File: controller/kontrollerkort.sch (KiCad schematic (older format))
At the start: 20 parts, among them J1 SPI, J2 SERIAL, J3 POWER, J4 RESET, J5 CONTROL, J6 SENSORS, U1 ATMEGA8

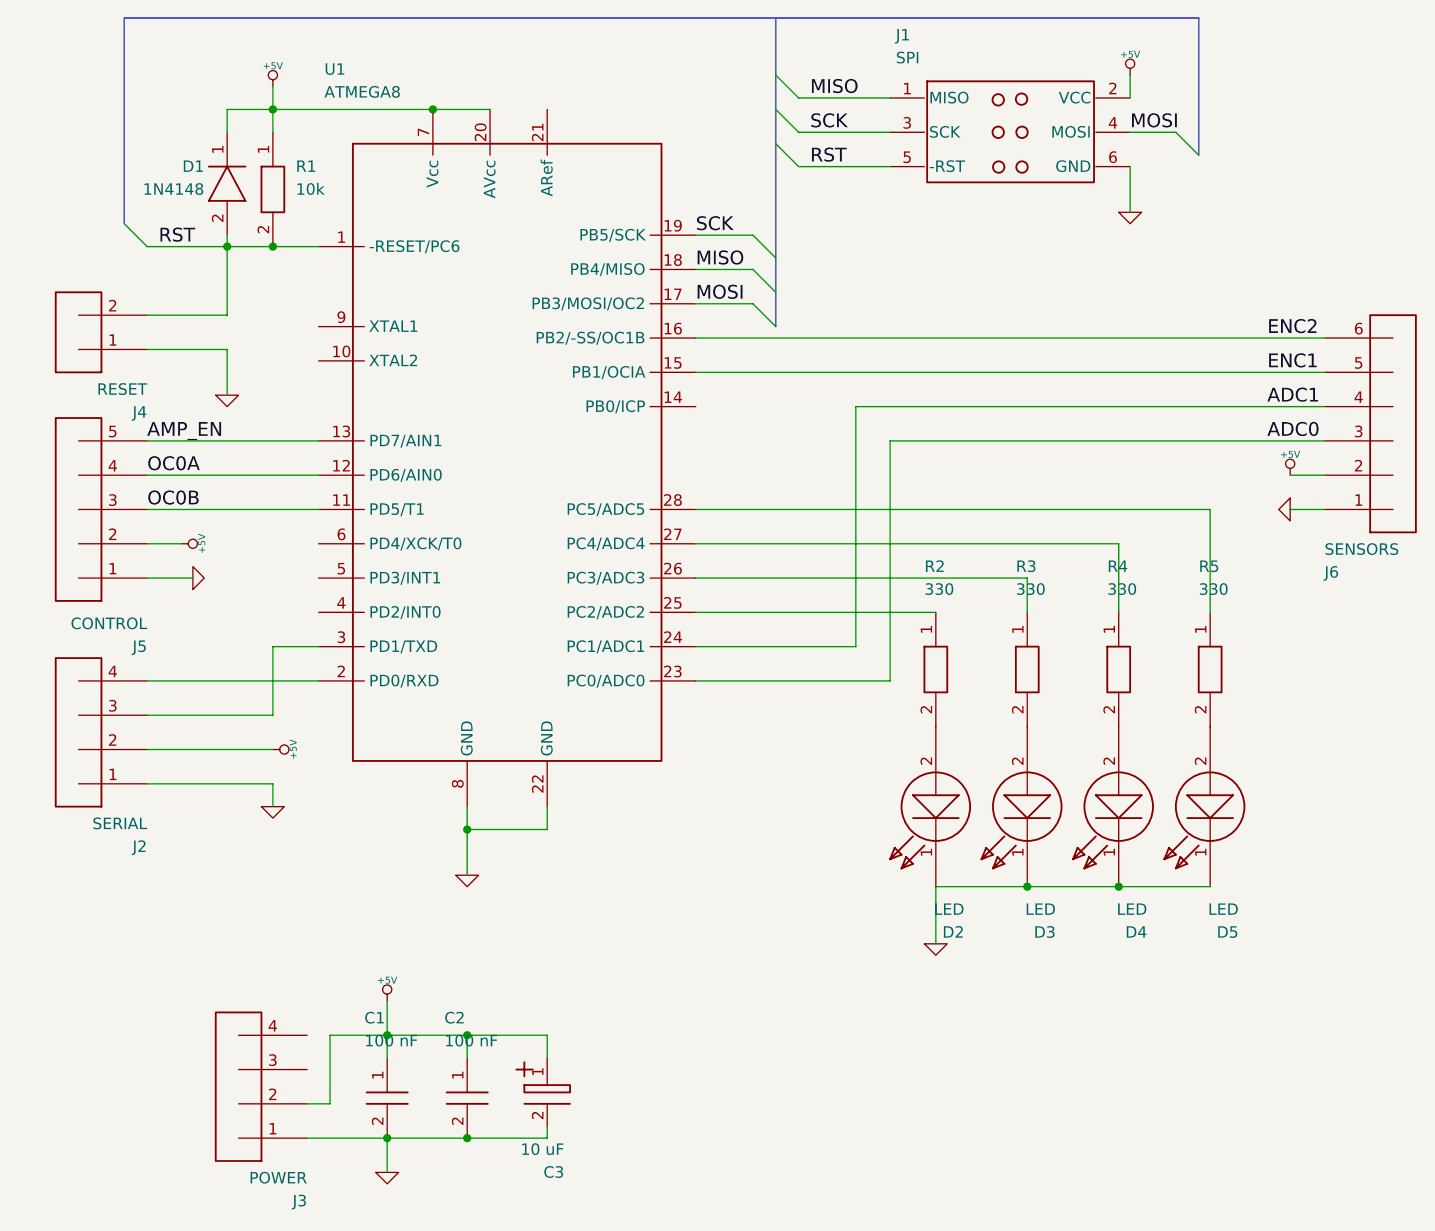
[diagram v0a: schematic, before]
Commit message: Updated controller board. Changed some connector pinouts to simplify board layout.
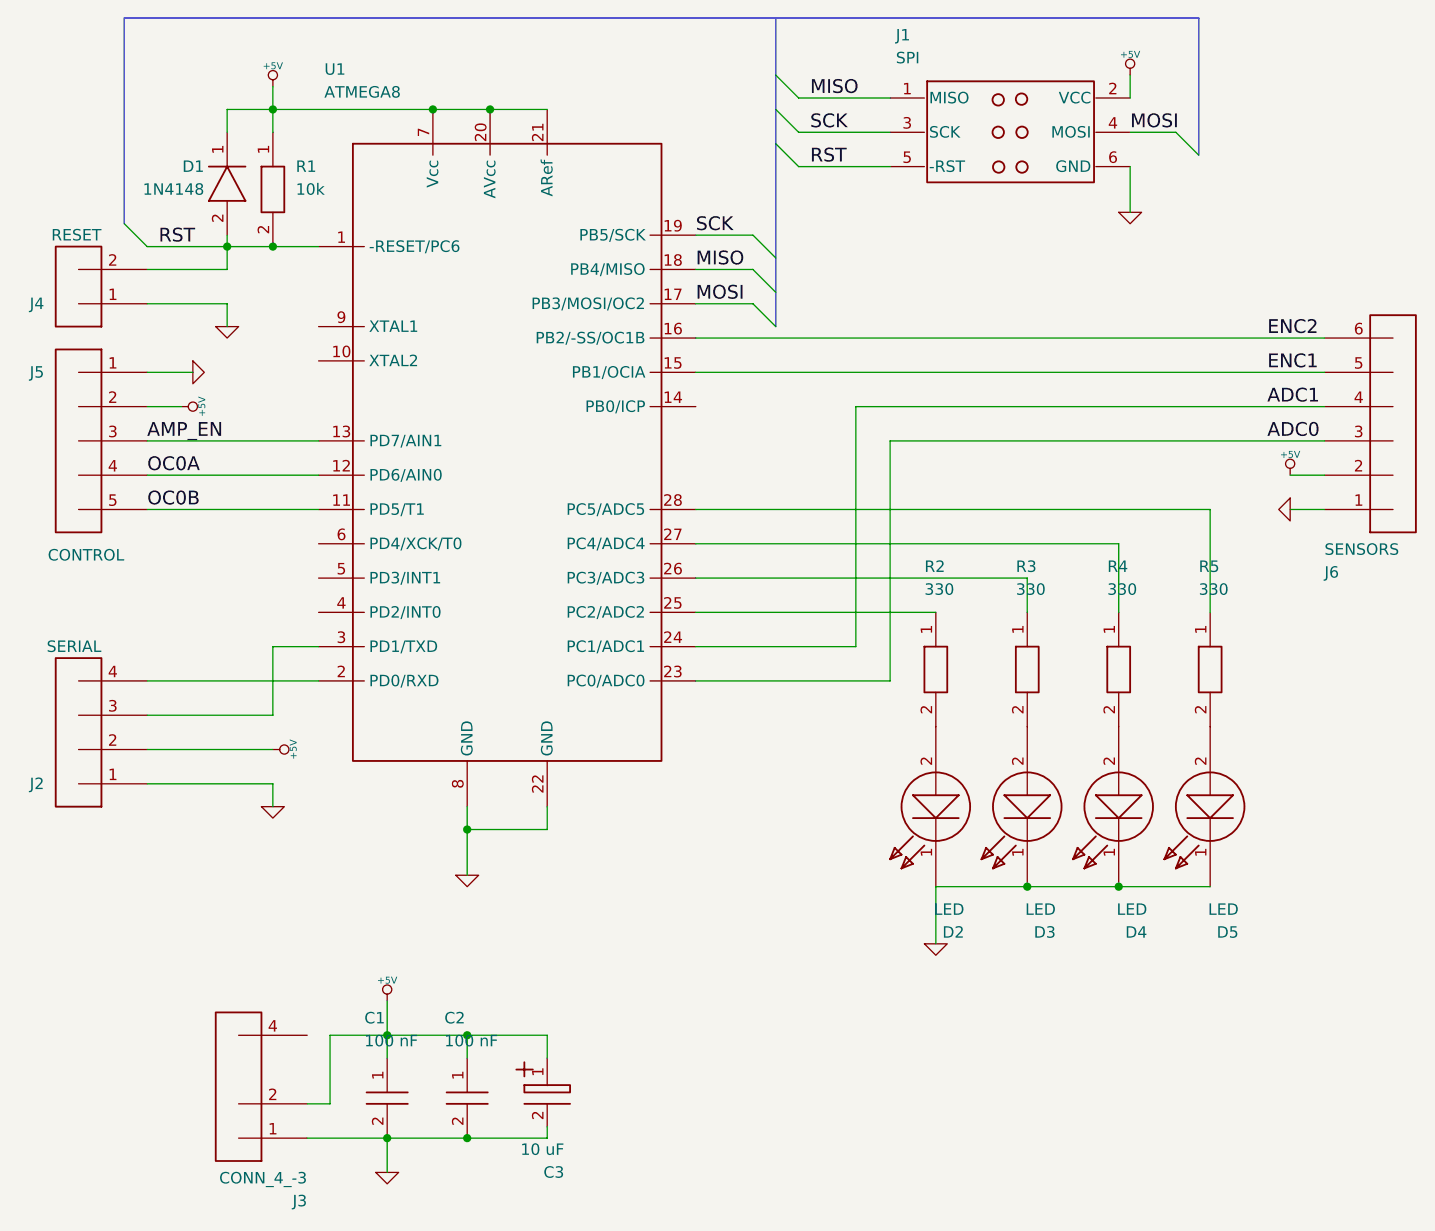
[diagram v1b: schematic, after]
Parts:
- removed J3: POWER, SIP4, symbol CONN_4
- added J3: CONN_4_-3, SIP4_-3, symbol CONN_4_-3
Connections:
- net +5V: now also U1.21 (ARef), J3.2
- net AMP_EN: now also J5.3; no longer J5.5
- net GND: now also J3.1
- net OC0B: now also J5.5; no longer J5.3
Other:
- moved on the sheet: J4, J5
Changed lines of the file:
@@
 LIBS:V_Relay
 LIBS:power
+LIBS:graphic
+LIBS:graphics
 LIBS:kontrollerkort-cache
 EELAYER 27 0
@@
 Sheet 1 1
 Title ""
-Date "7 oct 2014"
+Date "10 oct 2014"
 Rev ""
 Comp ""
@@
 $EndComp
 $Comp
-L +5V #PWR01
+L +5V #PWR4
 U 1 1 5433A0E3
 P 4300 2200
-F 0 "#PWR01" H 4300 2290 20  0001 C CNN
+F 0 "#PWR4" H 4300 2290 20  0001 C CNN
 F 1 "+5V" H 4300 2290 30  0000 C CNN
 F 2 "" H 4300 2200 60  0000 C CNN
@@
 $EndComp
 $Comp
-L GND #PWR02
+L GND #PWR9
 U 1 1 5433A107
 P 5150 5650
-F 0 "#PWR02" H 5150 5650 30  0001 C CNN
+F 0 "#PWR9" H 5150 5650 30  0001 C CNN
 F 1 "GND" H 5150 5580 30  0001 C CNN
 F 2 "" H 5150 5650 60  0000 C CNN
@@
 	6400 2850 6500 2950
 $Comp
-L GND #PWR03
+L GND #PWR12
 U 1 1 5433A632
 P 8050 2750
-F 0 "#PWR03" H 8050 2750 30  0001 C CNN
+F 0 "#PWR12" H 8050 2750 30  0001 C CNN
 F 1 "GND" H 8050 2680 30  0001 C CNN
 F 2 "" H 8050 2750 60  0000 C CNN
@@
 MISO
 $Comp
-L +5V #PWR04
+L +5V #PWR11
 U 1 1 5433B1B0
 P 8050 2150
-F 0 "#PWR04" H 8050 2240 20  0001 C CNN
+F 0 "#PWR11" H 8050 2240 20  0001 C CNN
 F 1 "+5V" H 8050 2240 30  0000 C CNN
 F 2 "" H 8050 2150 60  0000 C CNN
@@
 $EndComp
 $Comp
-L GND #PWR05
+L GND #PWR3
 U 1 1 5433B305
-P 4100 3550
-F 0 "#PWR05" H 4100 3550 30  0001 C CNN
-F 1 "GND" H 4100 3480 30  0001 C CNN
-F 2 "" H 4100 3550 60  0000 C CNN
-F 3 "" H 4100 3550 60  0000 C CNN
-	1    4100 3550
+P 4100 3250
+F 0 "#PWR3" H 4100 3250 30  0001 C CNN
+F 1 "GND" H 4100 3180 30  0001 C CNN
+F 2 "" H 4100 3250 60  0000 C CNN
+F 3 "" H 4100 3250 60  0000 C CNN
+	1    4100 3250
 	1    0    0    -1
 $EndComp
@@
 U 1 1 5433B4C6
 P 3550 5000
-F 0 "J2" H 3350 5525 50  0000 L CNN
-F 1 "SERIAL" H 3350 5425 50  0000 L CNN
+F 0 "J2" H 3800 5250 50  0000 L CNN
+F 1 "SERIAL" H 3550 4650 50  0000 L CNN
 F 2 "SIP4" H 3550 5000 50  0001 C CNN
 F 3 "" H 3550 5000 60  0000 C CNN
@@
 $EndComp
 $Comp
-L +5V #PWR06
+L +5V #PWR5
 U 1 1 5433B556
 P 4300 5100
-F 0 "#PWR06" H 4300 5190 20  0001 C CNN
+F 0 "#PWR5" H 4300 5190 20  0001 C CNN
 F 1 "+5V" H 4300 5190 30  0000 C CNN
 F 2 "" H 4300 5100 60  0000 C CNN
@@
 $EndComp
 $Comp
-L GND #PWR07
+L GND #PWR6
 U 1 1 5433B565
 P 4300 5350
-F 0 "#PWR07" H 4300 5350 30  0001 C CNN
+F 0 "#PWR6" H 4300 5350 30  0001 C CNN
 F 1 "GND" H 4300 5280 30  0001 C CNN
 F 2 "" H 4300 5350 60  0000 C CNN
@@
 $EndComp
 $Comp
-L GND #PWR08
+L GND #PWR8
 U 1 1 5433BBB4
 P 4800 6950
-F 0 "#PWR08" H 4800 6950 30  0001 C CNN
+F 0 "#PWR8" H 4800 6950 30  0001 C CNN
 F 1 "GND" H 4800 6880 30  0001 C CNN
 F 2 "" H 4800 6950 60  0000 C CNN
@@
 $EndComp
 $Comp
-L +5V #PWR09
+L +5V #PWR7
 U 1 1 5433BBC3
 P 4800 6200
-F 0 "#PWR09" H 4800 6290 20  0001 C CNN
+F 0 "#PWR7" H 4800 6290 20  0001 C CNN
 F 1 "+5V" H 4800 6290 30  0000 C CNN
 F 2 "" H 4800 6200 60  0000 C CNN
@@
 AMP_EN
 $Comp
-L +5V #PWR010
+L +5V #PWR1
 U 1 1 5433FABB
-P 3900 4200
-F 0 "#PWR010" H 3900 4290 20  0001 C CNN
-F 1 "+5V" H 3900 4290 30  0000 C CNN
-F 2 "" H 3900 4200 60  0000 C CNN
-F 3 "" H 3900 4200 60  0000 C CNN
-	1    3900 4200
-	0    1    1    0
-$EndComp
-$Comp
-L GND #PWR011
+P 3900 3600
+F 0 "#PWR1" H 3900 3690 20  0001 C CNN
+F 1 "+5V" H 3900 3690 30  0000 C CNN
+F 2 "" H 3900 3600 60  0000 C CNN
+F 3 "" H 3900 3600 60  0000 C CNN
+	1    3900 3600
+	0    1    -1   0
+$EndComp
+$Comp
+L GND #PWR2
 U 1 1 5433FACA
-P 3950 4350
-F 0 "#PWR011" H 3950 4350 30  0001 C CNN
-F 1 "GND" H 3950 4280 30  0001 C CNN
-F 2 "" H 3950 4350 60  0000 C CNN
-F 3 "" H 3950 4350 60  0000 C CNN
-	1    3950 4350
-	0    -1   -1   0
-$EndComp
-$Comp
-L CONN_4 J3
-U 1 1 5433FC65
-P 4250 6550
-F 0 "J3" H 4050 7075 50  0000 L CNN
-F 1 "POWER" H 4050 6975 50  0000 L CNN
-F 2 "SIP4" H 4250 6550 50  0001 C CNN
-F 3 "" H 4250 6550 60  0000 C CNN
-	1    4250 6550
-	-1   0    0    1
-$EndComp
-$Comp
-L GND #PWR012
+P 3950 3450
+F 0 "#PWR2" H 3950 3450 30  0001 C CNN
+F 1 "GND" H 3950 3380 30  0001 C CNN
+F 2 "" H 3950 3450 60  0000 C CNN
+F 3 "" H 3950 3450 60  0000 C CNN
+	1    3950 3450
+	0    -1   1    0
+$EndComp
+$Comp
+L GND #PWR14
 U 1 1 54340028
 P 8750 4050
-F 0 "#PWR012" H 8750 4050 30  0001 C CNN
+F 0 "#PWR14" H 8750 4050 30  0001 C CNN
 F 1 "GND" H 8750 3980 30  0001 C CNN
 F 2 "" H 8750 4050 60  0000 C CNN
@@
 $EndComp
 $Comp
-L +5V #PWR013
+L +5V #PWR13
 U 1 1 54340041
 P 8750 3900
-F 0 "#PWR013" H 8750 3990 20  0001 C CNN
+F 0 "#PWR13" H 8750 3990 20  0001 C CNN
 F 1 "+5V" H 8750 3990 30  0000 C CNN
 F 2 "" H 8750 3900 60  0000 C CNN
@@
 $EndComp
 $Comp
-L GND #PWR014
+L GND #PWR10
 U 1 1 54340947
 P 7200 5950
-F 0 "#PWR014" H 7200 5950 30  0001 C CNN
+F 0 "#PWR10" H 7200 5950 30  0001 C CNN
 F 1 "GND" H 7200 5880 30  0001 C CNN
 F 2 "" H 7200 5950 60  0000 C CNN
@@
 L CONN_5 J5
 U 1 1 543411BB
-P 3550 4050
-F 0 "J5" H 3350 4650 50  0000 L CNN
-F 1 "CONTROL" H 3350 4550 50  0000 L CNN
-F 2 "SIP5" H 3550 4050 50  0001 C CNN
-F 3 "" H 3550 4050 60  0000 C CNN
-	1    3550 4050
-	-1   0    0    1
+P 3550 3750
+F 0 "J5" H 3800 4050 50  0000 L CNN
+F 1 "CONTROL" H 3450 3250 50  0000 L CNN
+F 2 "SIP5" H 3550 3750 50  0001 C CNN
+F 3 "" H 3550 3750 60  0000 C CNN
+	1    3550 3750
+	-1   0    0    -1
 $EndComp
 Wire Wire Line
 	3750 2900 4500 2900
 Wire Wire Line
-	4100 2850 4100 3200
+	4100 2850 4100 3000
 Connection ~ 4300 2900
 Wire Wire Line
@@
 	4100 2400 4100 2300
 Wire Wire Line
-	4100 2300 5250 2300
+	4100 2300 5500 2300
 Connection ~ 4300 2300
 Wire Wire Line
@@
 	6150 3300 8900 3300
 Wire Wire Line
-	3750 4350 3950 4350
-Wire Wire Line
-	3750 4200 3900 4200
+	3750 3450 3950 3450
+Wire Wire Line
+	3750 3600 3900 3600
 Wire Wire Line
 	4550 6350 5500 6350
@@
 L CONN_2 J4
 U 1 1 543413A4
-P 3550 3250
-F 0 "J4" H 3350 3625 50  0000 L CNN
-F 1 "RESET" H 3350 3525 50  0000 L CNN
-F 2 "SIP2" H 3550 3250 50  0001 C CNN
-F 3 "" H 3550 3250 60  0000 C CNN
-	1    3550 3250
-	-1   0    0    1
-$EndComp
-Wire Wire Line
-	4100 3200 3750 3200
-Wire Wire Line
-	3750 3350 4100 3350
-Wire Wire Line
-	4100 3350 4100 3550
+P 3550 3050
+F 0 "J4" H 3800 3150 50  0000 L CNN
+F 1 "RESET" H 3550 2850 50  0000 L CNN
+F 2 "SIP2" H 3550 3050 50  0001 C CNN
+F 3 "" H 3550 3050 60  0000 C CNN
+	1    3550 3050
+	-1   0    0    1
+$EndComp
+Wire Wire Line
+	4100 3000 3750 3000
+Wire Wire Line
+	3750 3150 4100 3150
 Wire Wire Line
 	8900 3600 6850 3600
@@
 Text Label 8650 3300 0    60   ~ 0
 ENC2
+Connection ~ 5250 2300
+$Comp
+L CONN_4_-3 J3
+U 1 1 5437C9F0
+P 4250 6550
+F 0 "J3" H 4050 7075 50  0000 L CNN
+F 1 "CONN_4_-3" H 4050 6975 50  0000 L CNN
+F 2 "SIP4_-3" H 4250 6550 50  0001 C CNN
+F 3 "" H 4250 6550 60  0000 C CNN
+	1    4250 6550
+	-1   0    0    1
+$EndComp
+Wire Wire Line
+	4100 3150 4100 3250
 $EndSCHEMATC
